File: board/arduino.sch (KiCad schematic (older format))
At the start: 12 parts, among them J12 GND, J13 RX, J14 TX

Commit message: firmware changes to support toggle and momentary swithces. I have no idea what was the hardware modifications
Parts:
- A1: symbol MCU_Module:Arduino_Nano_v3.x -> interface-full-rescue:Arduino_Nano_v3.x-MCU_Module
- J12, J13, J14: symbol Connector_Generic:Conn_01x01 -> interface-full-rescue:Conn_01x01-Connector_Generic
- R2, R3, R4, R5, R6, R7, R8, R9: symbol Device:R -> interface-full-rescue:R-Device
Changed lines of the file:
@@
 $EndDescr
 $Comp
-L MCU_Module:Arduino_Nano_v3.x A1
+L interface-full-rescue:Arduino_Nano_v3.x-MCU_Module A1
 U 1 1 5E2ABF00
 P 3550 2250
@@
 AR Path="/5E3799FC/5E2ABF00" Ref="A2"  Part="1"
 AR Path="/5E37C631/5E2ABF00" Ref="A3"  Part="1"
+AR Path="/5E2ABF00" Ref="A2"  Part="1"
 F 0 "A2" H 3850 1250 50  0000 C CNN
 F 1 "Arduino" H 3950 1150 50  0000 C CNN
@@
 $EndComp
 $Comp
-L Device:R R2
+L interface-full-rescue:R-Device R2
 U 1 1 5E2D6FBB
 P 2050 3550
@@
 $EndComp
 $Comp
-L Device:R R6
+L interface-full-rescue:R-Device R6
 U 1 1 5E2D75EF
 P 2050 4450
@@
 	2550 3250 2050 3250
 $Comp
-L Device:R R3
+L interface-full-rescue:R-Device R3
 U 1 1 5E2E22DB
 P 2300 3550
@@
 $EndComp
 $Comp
-L Device:R R4
+L interface-full-rescue:R-Device R4
 U 1 1 5E2E2986
 P 2550 3550
@@
 $EndComp
 $Comp
-L Device:R R5
+L interface-full-rescue:R-Device R5
 U 1 1 5E2E2E54
 P 2800 3550
@@
 	2800 4200 2800 3700
 $Comp
-L Device:R R7
+L interface-full-rescue:R-Device R7
 U 1 1 5E2E6E3C
 P 2300 4450
@@
 $EndComp
 $Comp
-L Device:R R8
+L interface-full-rescue:R-Device R8
 U 1 1 5E2E6F85
 P 2550 4450
@@
 $EndComp
 $Comp
-L Device:R R9
+L interface-full-rescue:R-Device R9
 U 1 1 5E2E703C
 P 2800 4450
@@
 Connection ~ 2050 3900
 $Comp
-L power:GND #PWR013
+L interface-full-rescue:GND-power #PWR013
 U 1 1 5E2E97B2
 P 2050 4600
@@
 AR Path="/5E3799FC/5E2E97B2" Ref="#PWR026"  Part="1"
 AR Path="/5E37C631/5E2E97B2" Ref="#PWR039"  Part="1"
+AR Path="/5E2E97B2" Ref="#PWR026"  Part="1"
 F 0 "#PWR026" H 2050 4350 50  0001 C CNN
 F 1 "GND" H 2055 4427 50  0000 C CNN
@@
 $EndComp
 $Comp
-L power:GND #PWR014
+L interface-full-rescue:GND-power #PWR014
 U 1 1 5E2E9EE6
 P 2300 4600
@@
 AR Path="/5E3799FC/5E2E9EE6" Ref="#PWR027"  Part="1"
 AR Path="/5E37C631/5E2E9EE6" Ref="#PWR040"  Part="1"
+AR Path="/5E2E9EE6" Ref="#PWR027"  Part="1"
 F 0 "#PWR027" H 2300 4350 50  0001 C CNN
 F 1 "GND" H 2305 4427 50  0000 C CNN
@@
 $EndComp
 $Comp
-L power:GND #PWR015
+L interface-full-rescue:GND-power #PWR015
 U 1 1 5E2EA11A
 P 2550 4600
@@
 AR Path="/5E3799FC/5E2EA11A" Ref="#PWR028"  Part="1"
 AR Path="/5E37C631/5E2EA11A" Ref="#PWR041"  Part="1"
+AR Path="/5E2EA11A" Ref="#PWR028"  Part="1"
 F 0 "#PWR028" H 2550 4350 50  0001 C CNN
 F 1 "GND" H 2555 4427 50  0000 C CNN
@@
 $EndComp
 $Comp
-L power:GND #PWR016
+L interface-full-rescue:GND-power #PWR016
 U 1 1 5E2EA1CD
 P 2800 4600
@@
 AR Path="/5E3799FC/5E2EA1CD" Ref="#PWR029"  Part="1"
 AR Path="/5E37C631/5E2EA1CD" Ref="#PWR042"  Part="1"
+AR Path="/5E2EA1CD" Ref="#PWR029"  Part="1"
 F 0 "#PWR029" H 2800 4350 50  0001 C CNN
 F 1 "GND" H 2805 4427 50  0000 C CNN
@@
 $EndComp
 $Comp
-L power:+5V #PWR010
+L interface-full-rescue:+5V-power #PWR010
 U 1 1 5E2EA957
 P 3750 1100
@@
 AR Path="/5E3799FC/5E2EA957" Ref="#PWR023"  Part="1"
 AR Path="/5E37C631/5E2EA957" Ref="#PWR036"  Part="1"
+AR Path="/5E2EA957" Ref="#PWR023"  Part="1"
 F 0 "#PWR023" H 3750 950 50  0001 C CNN
 F 1 "+5V" H 3765 1273 50  0000 C CNN
@@
 	3750 1100 3750 1250
 $Comp
-L power:GND #PWR012
+L interface-full-rescue:GND-power #PWR012
 U 1 1 5E2EC0EE
 P 3550 3600
@@
 AR Path="/5E3799FC/5E2EC0EE" Ref="#PWR025"  Part="1"
 AR Path="/5E37C631/5E2EC0EE" Ref="#PWR038"  Part="1"
+AR Path="/5E2EC0EE" Ref="#PWR025"  Part="1"
 F 0 "#PWR025" H 3550 3350 50  0001 C CNN
 F 1 "GND" H 3555 3427 50  0000 C CNN
@@
 	3550 3350 3550 3600
 $Comp
-L Connector_Generic:Conn_01x01 J14
+L interface-full-rescue:Conn_01x01-Connector_Generic J14
 U 1 1 5E2EFE7E
 P 2250 1550
@@
 $EndComp
 $Comp
-L power:GND #PWR011
+L interface-full-rescue:GND-power #PWR011
 U 1 1 5E2F1EF0
 P 2700 1400
@@
 AR Path="/5E3799FC/5E2F1EF0" Ref="#PWR024"  Part="1"
 AR Path="/5E37C631/5E2F1EF0" Ref="#PWR037"  Part="1"
+AR Path="/5E2F1EF0" Ref="#PWR024"  Part="1"
 F 0 "#PWR024" H 2700 1150 50  0001 C CNN
 F 1 "GND" H 2705 1227 50  0001 C CNN
@@
 $EndComp
 $Comp
-L Connector_Generic:Conn_01x01 J13
+L interface-full-rescue:Conn_01x01-Connector_Generic J13
 U 1 1 5E2EEDF0
 P 2250 1450
@@
 $EndComp
 $Comp
-L Connector_Generic:Conn_01x01 J12
+L interface-full-rescue:Conn_01x01-Connector_Generic J12
 U 1 1 5E2F1B69
 P 2250 1350

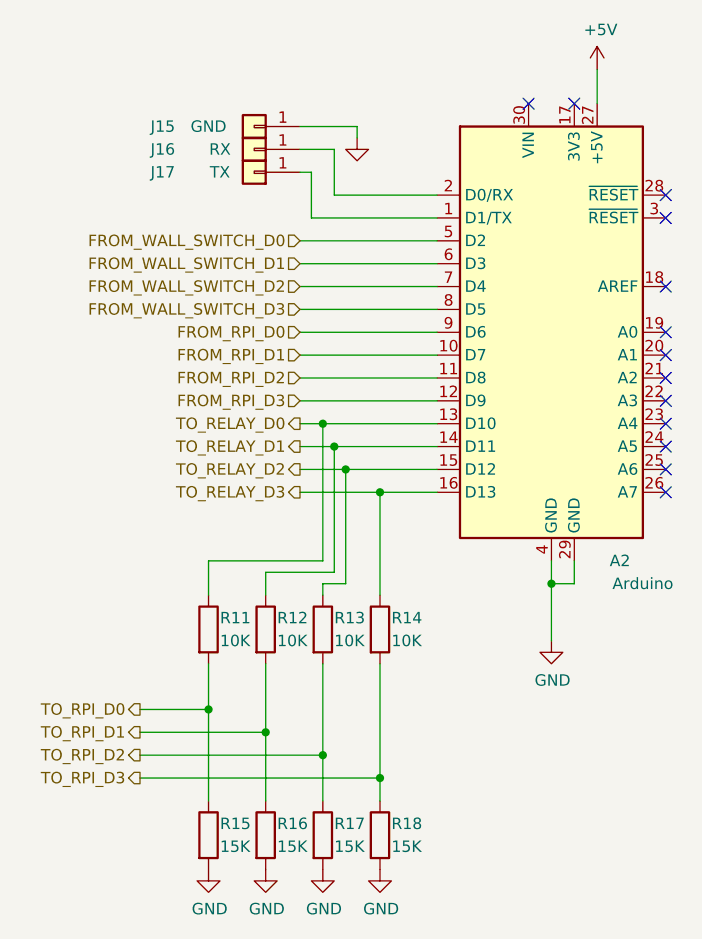
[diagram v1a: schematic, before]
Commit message: change sch to match rpi gpio numbering
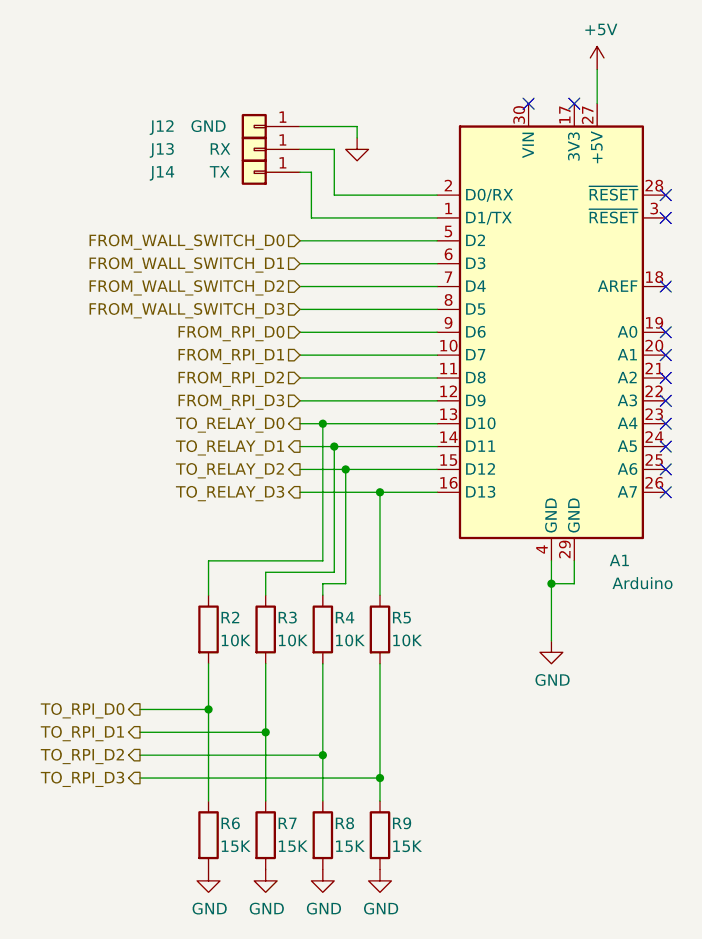
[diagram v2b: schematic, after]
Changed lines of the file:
@@
 $Descr A4 11693 8268
 encoding utf-8
-Sheet 3 4
+Sheet 2 4
 Title "Home Assistant Lighting Interface"
 Date "2020-01-30"
@@
 AR Path="/5E37C631/5E2ABF00" Ref="A3"  Part="1"
 AR Path="/5E2ABF00" Ref="A2"  Part="1"
-F 0 "A2" H 3850 1250 50  0000 C CNN
+F 0 "A1" H 3850 1250 50  0000 C CNN
 F 1 "Arduino" H 3950 1150 50  0000 C CNN
 F 2 "Module:Arduino_Nano" H 3550 2250 50  0001 C CIN
@@
 AR Path="/5E3799FC/5E2D6FBB" Ref="R11"  Part="1"
 AR Path="/5E37C631/5E2D6FBB" Ref="R20"  Part="1"
-F 0 "R11" H 2100 3600 50  0000 L CNN
+F 0 "R2" H 2100 3600 50  0000 L CNN
 F 1 "10K" H 2100 3500 50  0000 L CNN
 F 2 "Resistor_SMD:R_0805_2012Metric_Pad1.15x1.40mm_HandSolder" V 1980 3550 50  0001 C CNN
@@
 AR Path="/5E3799FC/5E2D75EF" Ref="R15"  Part="1"
 AR Path="/5E37C631/5E2D75EF" Ref="R24"  Part="1"
-F 0 "R15" H 2100 4500 50  0000 L CNN
+F 0 "R6" H 2100 4500 50  0000 L CNN
 F 1 "15K" H 2100 4400 50  0000 L CNN
 F 2 "Resistor_SMD:R_0805_2012Metric_Pad1.15x1.40mm_HandSolder" V 1980 4450 50  0001 C CNN
@@
 AR Path="/5E3799FC/5E2E22DB" Ref="R12"  Part="1"
 AR Path="/5E37C631/5E2E22DB" Ref="R21"  Part="1"
-F 0 "R12" H 2350 3600 50  0000 L CNN
+F 0 "R3" H 2350 3600 50  0000 L CNN
 F 1 "10K" H 2350 3500 50  0000 L CNN
 F 2 "Resistor_SMD:R_0805_2012Metric_Pad1.15x1.40mm_HandSolder" V 2230 3550 50  0001 C CNN
@@
 AR Path="/5E3799FC/5E2E2986" Ref="R13"  Part="1"
 AR Path="/5E37C631/5E2E2986" Ref="R22"  Part="1"
-F 0 "R13" H 2600 3600 50  0000 L CNN
+F 0 "R4" H 2600 3600 50  0000 L CNN
 F 1 "10K" H 2600 3500 50  0000 L CNN
 F 2 "Resistor_SMD:R_0805_2012Metric_Pad1.15x1.40mm_HandSolder" V 2480 3550 50  0001 C CNN
@@
 AR Path="/5E3799FC/5E2E2E54" Ref="R14"  Part="1"
 AR Path="/5E37C631/5E2E2E54" Ref="R23"  Part="1"
-F 0 "R14" H 2850 3600 50  0000 L CNN
+F 0 "R5" H 2850 3600 50  0000 L CNN
 F 1 "10K" H 2850 3500 50  0000 L CNN
 F 2 "Resistor_SMD:R_0805_2012Metric_Pad1.15x1.40mm_HandSolder" V 2730 3550 50  0001 C CNN
@@
 AR Path="/5E3799FC/5E2E6E3C" Ref="R16"  Part="1"
 AR Path="/5E37C631/5E2E6E3C" Ref="R25"  Part="1"
-F 0 "R16" H 2350 4500 50  0000 L CNN
+F 0 "R7" H 2350 4500 50  0000 L CNN
 F 1 "15K" H 2350 4400 50  0000 L CNN
 F 2 "Resistor_SMD:R_0805_2012Metric_Pad1.15x1.40mm_HandSolder" V 2230 4450 50  0001 C CNN
@@
 AR Path="/5E3799FC/5E2E6F85" Ref="R17"  Part="1"
 AR Path="/5E37C631/5E2E6F85" Ref="R26"  Part="1"
-F 0 "R17" H 2600 4500 50  0000 L CNN
+F 0 "R8" H 2600 4500 50  0000 L CNN
 F 1 "15K" H 2600 4400 50  0000 L CNN
 F 2 "Resistor_SMD:R_0805_2012Metric_Pad1.15x1.40mm_HandSolder" V 2480 4450 50  0001 C CNN
@@
 AR Path="/5E3799FC/5E2E703C" Ref="R18"  Part="1"
 AR Path="/5E37C631/5E2E703C" Ref="R27"  Part="1"
-F 0 "R18" H 2850 4500 50  0000 L CNN
+F 0 "R9" H 2850 4500 50  0000 L CNN
 F 1 "15K" H 2850 4400 50  0000 L CNN
 F 2 "Resistor_SMD:R_0805_2012Metric_Pad1.15x1.40mm_HandSolder" V 2730 4450 50  0001 C CNN
@@
 AR Path="/5E37C631/5E2E97B2" Ref="#PWR039"  Part="1"
 AR Path="/5E2E97B2" Ref="#PWR026"  Part="1"
-F 0 "#PWR026" H 2050 4350 50  0001 C CNN
+F 0 "#PWR039" H 2050 4350 50  0001 C CNN
 F 1 "GND" H 2055 4427 50  0000 C CNN
 F 2 "" H 2050 4600 50  0001 C CNN
@@
 AR Path="/5E37C631/5E2E9EE6" Ref="#PWR040"  Part="1"
 AR Path="/5E2E9EE6" Ref="#PWR027"  Part="1"
-F 0 "#PWR027" H 2300 4350 50  0001 C CNN
+F 0 "#PWR040" H 2300 4350 50  0001 C CNN
 F 1 "GND" H 2305 4427 50  0000 C CNN
 F 2 "" H 2300 4600 50  0001 C CNN
@@
 AR Path="/5E37C631/5E2EA11A" Ref="#PWR041"  Part="1"
 AR Path="/5E2EA11A" Ref="#PWR028"  Part="1"
-F 0 "#PWR028" H 2550 4350 50  0001 C CNN
+F 0 "#PWR041" H 2550 4350 50  0001 C CNN
 F 1 "GND" H 2555 4427 50  0000 C CNN
 F 2 "" H 2550 4600 50  0001 C CNN
@@
 AR Path="/5E37C631/5E2EA1CD" Ref="#PWR042"  Part="1"
 AR Path="/5E2EA1CD" Ref="#PWR029"  Part="1"
-F 0 "#PWR029" H 2800 4350 50  0001 C CNN
+F 0 "#PWR042" H 2800 4350 50  0001 C CNN
 F 1 "GND" H 2805 4427 50  0000 C CNN
 F 2 "" H 2800 4600 50  0001 C CNN
@@
 AR Path="/5E37C631/5E2EA957" Ref="#PWR036"  Part="1"
 AR Path="/5E2EA957" Ref="#PWR023"  Part="1"
-F 0 "#PWR023" H 3750 950 50  0001 C CNN
+F 0 "#PWR036" H 3750 950 50  0001 C CNN
 F 1 "+5V" H 3765 1273 50  0000 C CNN
 F 2 "" H 3750 1100 50  0001 C CNN
@@
 AR Path="/5E37C631/5E2EC0EE" Ref="#PWR038"  Part="1"
 AR Path="/5E2EC0EE" Ref="#PWR025"  Part="1"
-F 0 "#PWR025" H 3550 3350 50  0001 C CNN
+F 0 "#PWR038" H 3550 3350 50  0001 C CNN
 F 1 "GND" H 3555 3427 50  0000 C CNN
 F 2 "" H 3550 3600 50  0001 C CNN
@@
 AR Path="/5E3799FC/5E2EFE7E" Ref="J17"  Part="1"
 AR Path="/5E37C631/5E2EFE7E" Ref="J20"  Part="1"
-F 0 "J17" H 2650 1550 50  0000 C CNN
+F 0 "J14" H 2650 1550 50  0000 C CNN
 F 1 "TX" H 2400 1550 50  0000 C CNN
 F 2 "Connector_PinHeader_2.54mm:PinHeader_1x01_P2.54mm_Vertical" H 2250 1550 50  0001 C CNN
@@
 AR Path="/5E37C631/5E2F1EF0" Ref="#PWR037"  Part="1"
 AR Path="/5E2F1EF0" Ref="#PWR024"  Part="1"
-F 0 "#PWR024" H 2700 1150 50  0001 C CNN
+F 0 "#PWR037" H 2700 1150 50  0001 C CNN
 F 1 "GND" H 2705 1227 50  0001 C CNN
 F 2 "" H 2700 1400 50  0001 C CNN
@@
 AR Path="/5E3799FC/5E2EEDF0" Ref="J16"  Part="1"
 AR Path="/5E37C631/5E2EEDF0" Ref="J19"  Part="1"
-F 0 "J16" H 2650 1450 50  0000 C CNN
+F 0 "J13" H 2650 1450 50  0000 C CNN
 F 1 "RX" H 2400 1450 50  0000 C CNN
 F 2 "Connector_PinHeader_2.54mm:PinHeader_1x01_P2.54mm_Vertical" H 2250 1450 50  0001 C CNN
@@
 AR Path="/5E3799FC/5E2F1B69" Ref="J15"  Part="1"
 AR Path="/5E37C631/5E2F1B69" Ref="J18"  Part="1"
-F 0 "J15" H 2650 1350 50  0000 C CNN
+F 0 "J12" H 2650 1350 50  0000 C CNN
 F 1 "GND" H 2450 1350 50  0000 C CNN
 F 2 "Connector_PinHeader_2.54mm:PinHeader_1x01_P2.54mm_Vertical" H 2250 1350 50  0001 C CNN

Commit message: Fix RPI GPIO numbers
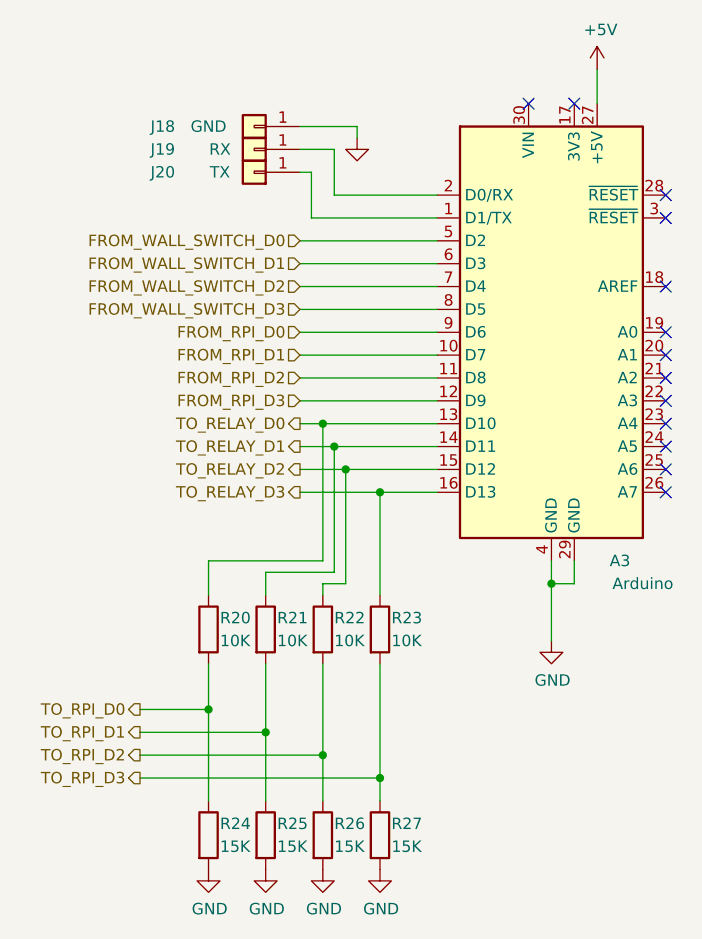
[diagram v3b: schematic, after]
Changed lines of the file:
@@
 $Descr A4 11693 8268
 encoding utf-8
-Sheet 2 4
+Sheet 4 4
 Title "Home Assistant Lighting Interface"
 Date "2020-01-30"
@@
 AR Path="/5E37C631/5E2ABF00" Ref="A3"  Part="1"
 AR Path="/5E2ABF00" Ref="A2"  Part="1"
-F 0 "A1" H 3850 1250 50  0000 C CNN
+F 0 "A3" H 3850 1250 50  0000 C CNN
 F 1 "Arduino" H 3950 1150 50  0000 C CNN
 F 2 "Module:Arduino_Nano" H 3550 2250 50  0001 C CIN
@@
 AR Path="/5E3799FC/5E2D6FBB" Ref="R11"  Part="1"
 AR Path="/5E37C631/5E2D6FBB" Ref="R20"  Part="1"
-F 0 "R2" H 2100 3600 50  0000 L CNN
+F 0 "R20" H 2100 3600 50  0000 L CNN
 F 1 "10K" H 2100 3500 50  0000 L CNN
 F 2 "Resistor_SMD:R_0805_2012Metric_Pad1.15x1.40mm_HandSolder" V 1980 3550 50  0001 C CNN
@@
 AR Path="/5E3799FC/5E2D75EF" Ref="R15"  Part="1"
 AR Path="/5E37C631/5E2D75EF" Ref="R24"  Part="1"
-F 0 "R6" H 2100 4500 50  0000 L CNN
+F 0 "R24" H 2100 4500 50  0000 L CNN
 F 1 "15K" H 2100 4400 50  0000 L CNN
 F 2 "Resistor_SMD:R_0805_2012Metric_Pad1.15x1.40mm_HandSolder" V 1980 4450 50  0001 C CNN
@@
 AR Path="/5E3799FC/5E2E22DB" Ref="R12"  Part="1"
 AR Path="/5E37C631/5E2E22DB" Ref="R21"  Part="1"
-F 0 "R3" H 2350 3600 50  0000 L CNN
+F 0 "R21" H 2350 3600 50  0000 L CNN
 F 1 "10K" H 2350 3500 50  0000 L CNN
 F 2 "Resistor_SMD:R_0805_2012Metric_Pad1.15x1.40mm_HandSolder" V 2230 3550 50  0001 C CNN
@@
 AR Path="/5E3799FC/5E2E2986" Ref="R13"  Part="1"
 AR Path="/5E37C631/5E2E2986" Ref="R22"  Part="1"
-F 0 "R4" H 2600 3600 50  0000 L CNN
+F 0 "R22" H 2600 3600 50  0000 L CNN
 F 1 "10K" H 2600 3500 50  0000 L CNN
 F 2 "Resistor_SMD:R_0805_2012Metric_Pad1.15x1.40mm_HandSolder" V 2480 3550 50  0001 C CNN
@@
 AR Path="/5E3799FC/5E2E2E54" Ref="R14"  Part="1"
 AR Path="/5E37C631/5E2E2E54" Ref="R23"  Part="1"
-F 0 "R5" H 2850 3600 50  0000 L CNN
+F 0 "R23" H 2850 3600 50  0000 L CNN
 F 1 "10K" H 2850 3500 50  0000 L CNN
 F 2 "Resistor_SMD:R_0805_2012Metric_Pad1.15x1.40mm_HandSolder" V 2730 3550 50  0001 C CNN
@@
 AR Path="/5E3799FC/5E2E6E3C" Ref="R16"  Part="1"
 AR Path="/5E37C631/5E2E6E3C" Ref="R25"  Part="1"
-F 0 "R7" H 2350 4500 50  0000 L CNN
+F 0 "R25" H 2350 4500 50  0000 L CNN
 F 1 "15K" H 2350 4400 50  0000 L CNN
 F 2 "Resistor_SMD:R_0805_2012Metric_Pad1.15x1.40mm_HandSolder" V 2230 4450 50  0001 C CNN
@@
 AR Path="/5E3799FC/5E2E6F85" Ref="R17"  Part="1"
 AR Path="/5E37C631/5E2E6F85" Ref="R26"  Part="1"
-F 0 "R8" H 2600 4500 50  0000 L CNN
+F 0 "R26" H 2600 4500 50  0000 L CNN
 F 1 "15K" H 2600 4400 50  0000 L CNN
 F 2 "Resistor_SMD:R_0805_2012Metric_Pad1.15x1.40mm_HandSolder" V 2480 4450 50  0001 C CNN
@@
 AR Path="/5E3799FC/5E2E703C" Ref="R18"  Part="1"
 AR Path="/5E37C631/5E2E703C" Ref="R27"  Part="1"
-F 0 "R9" H 2850 4500 50  0000 L CNN
+F 0 "R27" H 2850 4500 50  0000 L CNN
 F 1 "15K" H 2850 4400 50  0000 L CNN
 F 2 "Resistor_SMD:R_0805_2012Metric_Pad1.15x1.40mm_HandSolder" V 2730 4450 50  0001 C CNN
@@
 AR Path="/5E3799FC/5E2EFE7E" Ref="J17"  Part="1"
 AR Path="/5E37C631/5E2EFE7E" Ref="J20"  Part="1"
-F 0 "J14" H 2650 1550 50  0000 C CNN
+F 0 "J20" H 2650 1550 50  0000 C CNN
 F 1 "TX" H 2400 1550 50  0000 C CNN
 F 2 "Connector_PinHeader_2.54mm:PinHeader_1x01_P2.54mm_Vertical" H 2250 1550 50  0001 C CNN
@@
 AR Path="/5E3799FC/5E2EEDF0" Ref="J16"  Part="1"
 AR Path="/5E37C631/5E2EEDF0" Ref="J19"  Part="1"
-F 0 "J13" H 2650 1450 50  0000 C CNN
+F 0 "J19" H 2650 1450 50  0000 C CNN
 F 1 "RX" H 2400 1450 50  0000 C CNN
 F 2 "Connector_PinHeader_2.54mm:PinHeader_1x01_P2.54mm_Vertical" H 2250 1450 50  0001 C CNN
@@
 AR Path="/5E3799FC/5E2F1B69" Ref="J15"  Part="1"
 AR Path="/5E37C631/5E2F1B69" Ref="J18"  Part="1"
-F 0 "J12" H 2650 1350 50  0000 C CNN
+F 0 "J18" H 2650 1350 50  0000 C CNN
 F 1 "GND" H 2450 1350 50  0000 C CNN
 F 2 "Connector_PinHeader_2.54mm:PinHeader_1x01_P2.54mm_Vertical" H 2250 1350 50  0001 C CNN
